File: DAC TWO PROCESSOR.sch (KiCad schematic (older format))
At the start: 99 parts

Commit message: Added outline, mounting holes and annotated components.
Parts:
- added H1, H2: MountingHole_Pad, symbol Mechanical:MountingHole_Pad
- J1: renamed from J?; symbol SciLib:CONN_20 -> DAC-TWO-PROCESSOR-rescue:CONN_20-SciLib
- J2: renamed from J?; symbol SciLib:CONN_10x2 -> DAC-TWO-PROCESSOR-rescue:CONN_10x2-SciLib
- J3: renamed from J?; symbol SciLib:CONN_10 -> DAC-TWO-PROCESSOR-rescue:CONN_10-SciLib
- U1: renamed from U?; symbol SciLib:ADP5070 -> DAC-TWO-PROCESSOR-rescue:ADP5070-SciLib
- U10: renamed from U?; symbol SciLib:LT1964-SD -> DAC-TWO-PROCESSOR-rescue:LT1964-SD-SciLib
- U11: renamed from U?; symbol SciLib:SM78L05 -> DAC-TWO-PROCESSOR-rescue:SM78L05-SciLib
- U12: renamed from U?; symbol SciLib:SM79L05 -> DAC-TWO-PROCESSOR-rescue:SM79L05-SciLib
- U2: renamed from U?; symbol SciLib:REG113-3.3 -> DAC-TWO-PROCESSOR-rescue:REG113-3.3-SciLib
- U3: renamed from U?; symbol SciLib:XTALOSC -> DAC-TWO-PROCESSOR-rescue:XTALOSC-SciLib
- U4: renamed from U?; symbol SciLib:ADP7118 -> DAC-TWO-PROCESSOR-rescue:ADP7118-SciLib
- U5: renamed from U?; symbol SciLib:AT25160B -> DAC-TWO-PROCESSOR-rescue:AT25160B-SciLib
- U6: renamed from U?; symbol SciLib:ADP7182 -> DAC-TWO-PROCESSOR-rescue:ADP7182-SciLib
- U7: renamed from U?; symbol SciLib:STM32F7xx -> DAC-TWO-PROCESSOR-rescue:STM32F7xx-SciLib
- U8, U9: renamed from U?; symbol SciLib:LT1763CS8 -> DAC-TWO-PROCESSOR-rescue:LT1763CS8-SciLib
- UX1: renamed from UX?; symbol SciLib:LT1010CN -> DAC-TWO-PROCESSOR-rescue:LT1010CN-SciLib
- gave numbers to parts that had none: 83
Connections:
- no-connect marks 34 -> 36

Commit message: Pushing footprints
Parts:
- U3: footprint CB3 -> (none)
- UX1: footprint DIP8P -> (none)
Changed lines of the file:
@@
 F 0 "U3" H 6050 2587 60  0000 C CNN
 F 1 "XX MHz" H 6050 2481 60  0000 C CNN
-F 2 "CB3" H 6050 1900 60  0001 C CNN
+F 2 "" H 6050 1900 60  0001 C CNN
 F 3 "std_library/doc/discrete/CTS CB3 OSC.pdf" H 6050 2587 60  0001 C CNN
 F 4 "11690" H 6050 2481 60  0001 C CNN "Partnum"
@@
 F 0 "UX1" H 15800 6250 60  0000 L CNN
 F 1 "LT1010CN" H 15800 6150 60  0000 L CNN
-F 2 "DIP8P" H 16050 5900 60  0001 C CNN
+F 2 "" H 16050 5900 60  0001 C CNN
 F 3 "std_library/doc/linear-tec/LT1010fc.pdf" H 16144 5947 60  0001 L CNN
 F 4 "11005" H 16144 5894 60  0001 L CNN "Partnum"

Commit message: Starting layout. Initial Commit.
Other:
- note added: "This footprint is wrong pinout! \nCorrect if using 8-lead LFCSP"
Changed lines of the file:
@@
 F 1 "LT1763CS8" H 9550 6774 50  0000 C CNN
 F 2 "" H 9550 6400 50  0001 C CNN
-F 3 "" H 9550 6400 50  0001 C CNN
+F 3 "https://www.analog.com/media/en/technical-documentation/data-sheets/1763fh.pdf" H 9550 6400 50  0001 C CNN
 	1    9550 6400
 	1    0    0    -1
@@
 F 1 "LT1964-SD" H 9675 10124 50  0000 C CNN
 F 2 "" H 9650 9700 50  0001 C CNN
-F 3 "" H 9650 9700 50  0001 C CNN
+F 3 "https://www.analog.com/media/en/technical-documentation/data-sheets/1964fb.pdf" H 9650 9700 50  0001 C CNN
 	1    9650 9700
 	1    0    0    -1
@@
 F 1 "LT1763CS8" H 9550 8424 50  0000 C CNN
 F 2 "" H 9550 8050 50  0001 C CNN
-F 3 "" H 9550 8050 50  0001 C CNN
+F 3 "https://www.analog.com/media/en/technical-documentation/data-sheets/1763fh.pdf" H 9550 8050 50  0001 C CNN
 	1    9550 8050
 	1    0    0    -1
@@
 NoConn ~ 1000 4600
 NoConn ~ 1000 5000
+Text Notes 5750 8550 0    59   Italic 12
+This footprint is wrong pinout! \nCorrect if using 8-lead LFCSP
 $EndSCHEMATC

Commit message: Layed out some more power rails. Need to TRIPLE check the EPAD connections. Many are incorrectly pinned.
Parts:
- removed U4: ADP7118, SciMod:ADP7118ARDZ, symbol DAC-TWO-PROCESSOR-rescue:ADP7118-SciLib
- added U4: ADP7118, Package_SO:SOIC-8-1EP_3.9x4.9mm_P1.27mm_EP2.35x2.35mm, symbol SciLib:ADP7118
- H1, H2: footprint (none) -> MountingHole:MountingHole_5mm_Pad_Via
- U10: footprint (none) -> SciMod:SOT23-5
- U8, U9: footprint (none) -> SciMod:SO-8_S
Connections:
- wire segments 559 -> 558
- no-connect marks 36 -> 34
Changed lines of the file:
@@
 NoConn ~ 15700 8300
-$Comp
-L DAC-TWO-PROCESSOR-rescue:ADP7118-SciLib U4
-U 1 1 5DE8A806
-P 6400 6750
-F 0 "U4" H 6500 7165 50  0000 C CNN
-F 1 "ADP7118" H 6500 7074 50  0000 C CNN
-F 2 "SciMod:ADP7118ARDZ" H 6400 6750 50  0001 C CNN
-F 3 "" H 6400 6750 50  0001 C CNN
-	1    6400 6750
-	1    0    0    -1
-$EndComp
 $Comp
 L DAC-TWO-PROCESSOR-rescue:ADP7182-SciLib U6
@@
 F 0 "U8" H 9550 6865 50  0000 C CNN
 F 1 "LT1763CS8" H 9550 6774 50  0000 C CNN
-F 2 "" H 9550 6400 50  0001 C CNN
+F 2 "SciMod:SO-8_S" H 9550 6400 50  0001 C CNN
 F 3 "https://www.analog.com/media/en/technical-documentation/data-sheets/1763fh.pdf" H 9550 6400 50  0001 C CNN
 	1    9550 6400
@@
 F 0 "U10" H 9675 10215 50  0000 C CNN
 F 1 "LT1964-SD" H 9675 10124 50  0000 C CNN
-F 2 "" H 9650 9700 50  0001 C CNN
+F 2 "SciMod:SOT23-5" H 9650 9700 50  0001 C CNN
 F 3 "https://www.analog.com/media/en/technical-documentation/data-sheets/1964fb.pdf" H 9650 9700 50  0001 C CNN
 	1    9650 9700
@@
 F 0 "U9" H 9550 8515 50  0000 C CNN
 F 1 "LT1763CS8" H 9550 8424 50  0000 C CNN
-F 2 "" H 9550 8050 50  0001 C CNN
+F 2 "SciMod:SO-8_S" H 9550 8050 50  0001 C CNN
 F 3 "https://www.analog.com/media/en/technical-documentation/data-sheets/1763fh.pdf" H 9550 8050 50  0001 C CNN
 	1    9550 8050
@@
 Connection ~ 10550 7200
 Wire Wire Line
-	10900 8500 10900 8550
-Wire Wire Line
 	10900 8800 10550 8800
-Connection ~ 10900 8550
 Wire Wire Line
 	10900 8550 10900 8800
@@
 F 0 "H2" H 1100 4949 50  0000 L CNN
 F 1 "MountingHole_Pad" H 1100 4858 50  0000 L CNN
-F 2 "" H 1000 4900 50  0001 C CNN
+F 2 "MountingHole:MountingHole_5mm_Pad_Via" H 1000 4900 50  0001 C CNN
 F 3 "~" H 1000 4900 50  0001 C CNN
 	1    1000 4900
@@
 F 0 "H1" H 1100 4549 50  0000 L CNN
 F 1 "MountingHole_Pad" H 1100 4458 50  0000 L CNN
-F 2 "" H 1000 4500 50  0001 C CNN
+F 2 "MountingHole:MountingHole_5mm_Pad_Via" H 1000 4500 50  0001 C CNN
 F 3 "~" H 1000 4500 50  0001 C CNN
 	1    1000 4500
 	1    0    0    -1
 $EndComp
-NoConn ~ 1000 4600
-NoConn ~ 1000 5000
 Text Notes 5750 8550 0    59   Italic 12
 This footprint is wrong pinout! \nCorrect if using 8-lead LFCSP
+$Comp
+L DAC-TWO-PROCESSOR-rescue:CM_GND-SciLib #PWR0158
+U 1 1 5DDC1768
+P 1000 5000
+F 0 "#PWR0158" H 1000 5050 40  0001 C CNN
+F 1 "CM_GND" H 986 5083 60  0001 C CNN
+F 2 "" H 1000 5000 60  0000 C CNN
+F 3 "" H 1000 5000 60  0000 C CNN
+	1    1000 5000
+	1    0    0    -1
+$EndComp
+$Comp
+L DAC-TWO-PROCESSOR-rescue:CM_GND-SciLib #PWR0159
+U 1 1 5DE1B7ED
+P 1000 4600
+F 0 "#PWR0159" H 1000 4650 40  0001 C CNN
+F 1 "CM_GND" H 986 4683 60  0001 C CNN
+F 2 "" H 1000 4600 60  0000 C CNN
+F 3 "" H 1000 4600 60  0000 C CNN
+	1    1000 4600
+	1    0    0    -1
+$EndComp
+$Comp
+L SciLib:ADP7118 U4
+U 1 1 5DFCFB62
+P 6400 6750
+F 0 "U4" H 6500 7165 50  0000 C CNN
+F 1 "ADP7118" H 6500 7074 50  0000 C CNN
+F 2 "Package_SO:SOIC-8-1EP_3.9x4.9mm_P1.27mm_EP2.35x2.35mm" H 6400 6750 50  0001 C CNN
+F 3 "" H 6400 6750 50  0001 C CNN
+	1    6400 6750
+	1    0    0    -1
+$EndComp
 $EndSCHEMATC

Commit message: Add files via upload
Final - added testpoints, added MANF# data. Removed reconstruction filter
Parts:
- removed C14: 4.7uF, SciMod:EIA0603, symbol Device:C
- removed C15: 10uF, SciMod:EIA1210, symbol Device:C
- removed C16, C17, C27, C41, C42: .1uF, SciMod:EIA0603, symbol Device:C
- removed C18, C19: 1uF, SciMod:EIA0603, symbol Device:C
- removed C20, C21, C22, C23, C24, C25: .01uF, SciMod:EIA0603, symbol Device:C
- removed C28: 2.2uF, SciMod:EIA0603, symbol Device:C
- removed C36, C37: 10uF, SciMod:EIA0805, symbol Device:C
- removed C39, C40, C43: .33uF, SciMod:EIA0603, symbol Device:C
- removed H1, H2: MountingHole_Pad, MountingHole:MountingHole_5mm_Pad_Via, symbol Mechanical:MountingHole_Pad
- removed R13, R14: 10, SciMod:EIA0603, symbol Device:R
- removed R15: 105K, SciMod:EIA0603, symbol Device:R
- removed R16: 10K, SciMod:EIA0603, symbol Device:R
- removed R19, R27, R28, R29, R30, R31, R32, R33, R34: 10K, SciMod:EIA0805, symbol Device:R
- removed U4: ADP7118, Package_SO:SOIC-8-1EP_3.9x4.9mm_P1.27mm_EP2.35x2.35mm, symbol SciLib:ADP7118
- removed UX1: LT1010CN, symbol DAC-TWO-PROCESSOR-rescue:LT1010CN-SciLib
- added C? (x3): 10uF, SciMod:EIA0805, symbol Device:C
- added C? (x3): .1uF, SciMod:EIA0603, symbol Device:C
- added C? (x5): .01uF, SciMod:EIA0603, symbol Device:C
- added C?: 4.7uF, SciMod:EIA0603, symbol Device:C
- added C? (x2): 1uF, SciMod:EIA0603, symbol Device:C
- added C?: 2.2uF, SciMod:EIA0603, symbol Device:C
- added C? (x3): .33uF, SciMod:EIA0603, symbol Device:C
- added R? (x9): 10K, SciMod:EIA0805, symbol Device:R
- added R? (x2): 10, SciMod:EIA0603, symbol Device:R
- added R?: 105K, SciMod:EIA0603, symbol Device:R
- added R?: 10K, SciMod:EIA0603, symbol Device:R
- added TP?: VOUT1, TESTPOINT, symbol SciLib:TST
- added TP?: +2.5V, TESTPOINT, symbol SciLib:TST
- added TP?: +8V, TESTPOINT, symbol SciLib:TST
- added TP?: -3V, TESTPOINT, symbol SciLib:TST
- added TP?: VOUT2, TESTPOINT, symbol SciLib:TST
- added U?: ADP7118, SciMod:ADP7118ARDZ, symbol SciLib:ADP7118
- C?: renamed from C4; footprint SciMod:EIA1210 -> SciMod:EIA0805; Field5 (none) -> 10µF ±10% 10V Ceramic Capacitor X7R 0805; MANF# (none) -> GRM21BR71A106KA73K
- C?: renamed from C2; Field5 (none) -> CAP CER 0.1UF 25V X8R 0603; MANF# (none) -> C1608X8R1E104K080AA
- C?: renamed from C13; Field5 (none) -> 10000pF ±5% 50V Ceramic Capacitor X7R 0805; MANF# (none) -> C0805C103J5RAC7210
- C?: renamed from C38; MANF# (none) -> CC0603KRX7R7BB334
- C?: renamed from C1; Field5 (none) -> 1µF ±20% 16V Ceramic Capacitor X7R 0603; MANF# (none) -> CL10B105MO8NNWC
- C?: renamed from C3; Field5 (none) -> 10µF Molded Tantalum Capacitors 10V 0805; MANF# (none) -> TACH106M010XTA
- C?: renamed from C7; Field4 (none) -> 2238 867 15279
- C?: renamed from C10; MANF# (none) -> 0603YC223KAT2A
- C?: renamed from C8; MANF# (none) -> CC0603JRNP09BN220
- C?: renamed from C9; MANF# (none) -> C3216X7R1H475M160AC
- C?: renamed from C6; MANF# (none) -> JMK107B7105MA
- C?: renamed from C5; MANF# (none) -> C3216X7R1E225K
- C?: renamed from C12; MANF# (none) -> C3216X7R1E225K
- C?: renamed from C11; MANF# (none) -> CL10B823KO8NNNC
- C?: renamed from C29; MANF# (none) -> GRM21BR71E225KA73L
- C?: renamed from C26; Field4 (none) -> C0603C475K9PACTU; Field5 (none) -> 4.7µF ±10% 6.3V Ceramic Capacitor X5R 0603
- C?: renamed from C35; MANF# (none) -> GRM21BR71A106KA73K
- D?: renamed from D2; MANF# (none) -> DFLS130-7
- D?: renamed from D1; MANF# (none) -> BAT54LPS
- J?: renamed from J2; symbol DAC-TWO-PROCESSOR-rescue:CONN_10x2-SciLib -> SciLib:CONN_10x2; MANF# (none) -> FTSH-110-01-L-DV; Mfg Pn FTSH-110-01-L-DV -> (none); Partnum 12133 -> (none)
- J?: renamed from J1; symbol DAC-TWO-PROCESSOR-rescue:CONN_20-SciLib -> SciLib:CONN_20; MANF# (none) -> Scientech supplied & installed; Mfg SCIENTECH -> (none)
- J?: renamed from J3; symbol DAC-TWO-PROCESSOR-rescue:CONN_10-SciLib -> SciLib:CONN_10; Description ?????? -> (none); MANF# (none) -> Scientech supplied & installed; Partnum XXXXX -> (none)
- L?: renamed from L4; MANF# (none) -> XFL4020-152MEB
- L?: renamed from L2; MANF# (none) -> LPS6235-153MRB
- L?: renamed from L1; MANF# (none) -> LPS6235-682MRB
- L?: renamed from L3; MANF# (none) -> LPS4018-222MRB
- R?: renamed from R20; Field5 (none) -> 10 kOhms ±5% 0.125W, 1/8W Chip Resistor 0805; MANF# (none) -> RMCF0805JT10K0
- R?: renamed from R1; Field5 (none) -> 30.1 kOhms ±1% 0.1W, 1/10W Chip Resistor 0603; MANF# (none) -> ERJ-3EKF3012V
- R?: renamed from R2; Field5 (none) -> 18.7 kOhms ±1% 0.1W, 1/10W Chip Resistor 0603; MANF# (none) -> ERJ-3EKF1872V
- R?: renamed from R3; Field5 (none) -> 49.9 kOhms ±1% 0.1W, 1/10W Chip Resistor 0603; MANF# (none) -> ERJ-3EKF4992V
- R?: renamed from R6; MANF# (none) -> CRCW060322K0FKEA
- R?: renamed from R7; MANF# (none) -> ERJ-3EKF3012V
- R?: renamed from R9; Field4 (none) -> ERJ-3RQF4R7V
- R?: renamed from R10; MANF# (none) -> ERJ2RKF6342X
- R?: renamed from R11; MANF# (none) -> ERJ-2RKF3571X
- R?: renamed from R4; MANF# (none) -> ERJ-2RKF2801X
- R?: renamed from R5; MANF# (none) -> ERJ-2RKF5492X
- R?: renamed from R8; MANF# (none) -> ERJ-3EKF10R0V
- R?: renamed from R17; MANF# (none) -> ERJ-3EKF1053V
- R?: renamed from R18; MANF# (none) -> ERJ-3EKF1002V
- R?: renamed from R12; MANF# (none) -> Scientech supplied & installed
- U?: renamed from U2; symbol DAC-TWO-PROCESSOR-rescue:REG113-3.3-SciLib -> SciLib:REG113-3.3; MANF# (none) -> REG113EA-3.3; Mfg Pn REG113EA-3.3 -> (none)
- U?: renamed from U5; symbol DAC-TWO-PROCESSOR-rescue:AT25160B-SciLib -> SciLib:AT25160B; MANF# (none) -> AT25160B-XHL-B; Mfg Pn AT25160B-XHL-B -> (none)
- U?: renamed from U11; symbol DAC-TWO-PROCESSOR-rescue:SM78L05-SciLib -> SciLib:SM78L05
- U?: renamed from U12; symbol DAC-TWO-PROCESSOR-rescue:SM79L05-SciLib -> SciLib:SM79L05
- U?: renamed from U1; symbol DAC-TWO-PROCESSOR-rescue:ADP5070-SciLib -> SciLib:ADP5070; MANF# (none) -> ADP5070ACPZ-R7
- U?: renamed from U6; symbol DAC-TWO-PROCESSOR-rescue:ADP7182-SciLib -> SciLib:ADP7182; Field4 (none) -> ADP7182ACPZN
- U?: renamed from U8; footprint SciMod:SO-8_S -> (none); symbol DAC-TWO-PROCESSOR-rescue:LT1763CS8-SciLib -> SciLib:LT1763CS8; MANF# (none) -> LT1763CS8#TRPBF
- U?: renamed from U10; footprint SciMod:SOT23-5 -> (none); symbol DAC-TWO-PROCESSOR-rescue:LT1964-SD-SciLib -> SciLib:LT1964-SD
- U?: renamed from U9; footprint SciMod:SO-8_S -> (none); symbol DAC-TWO-PROCESSOR-rescue:LT1763CS8-SciLib -> SciLib:LT1763CS8; MANF# (none) -> LT1763CS8#TRPBF
- U?: renamed from U7; symbol DAC-TWO-PROCESSOR-rescue:STM32F7xx-SciLib -> SciLib:STM32F7xx; MANF# (none) -> STM32F730R8T6
- U?: renamed from U3; footprint (none) -> CB3; symbol DAC-TWO-PROCESSOR-rescue:XTALOSC-SciLib -> SciLib:XTALOSC; MANF# (none) -> Scientech supplied & installed
- renumbered C30 to C?, C33 to C?, C31 to C?, C34 to C?, C32 to C?, R23 to R?, R24 to R?, R25 to R?, R26 to R?, R21 to R?, R22 to R?
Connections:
- wire segments 558 -> 542
- no-connect marks 34 -> 32
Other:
- note added: "From the AD5791 EVAL board."
- note added: "From the DC2222A LTC2500-32 A/D eval schematic"
- note removed: "This footprint is wrong pinout! \nCorrect if using 8-lead LFCSP"

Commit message: Added footpritn associations.
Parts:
- TP1, TP2, TP3, TP4, TP5: renamed from TP?; footprint TESTPOINT -> TestPoint:TestPoint_Keystone_5010-5014_Multipurpose
- U10: renamed from U?; footprint (none) -> SciMod:SOT23-5
- U3: renamed from U?; footprint CB3 -> SciMod:CB3
- U4: renamed from U?; symbol SciLib:ADP7118 -> DAC-TWO-PROCESSOR-rescue:ADP7118-SciLib
- U8, U9: renamed from U?; footprint (none) -> SciMod:SO-8_S
- gave numbers to parts that had none: 90
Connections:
- wire segments 542 -> 541

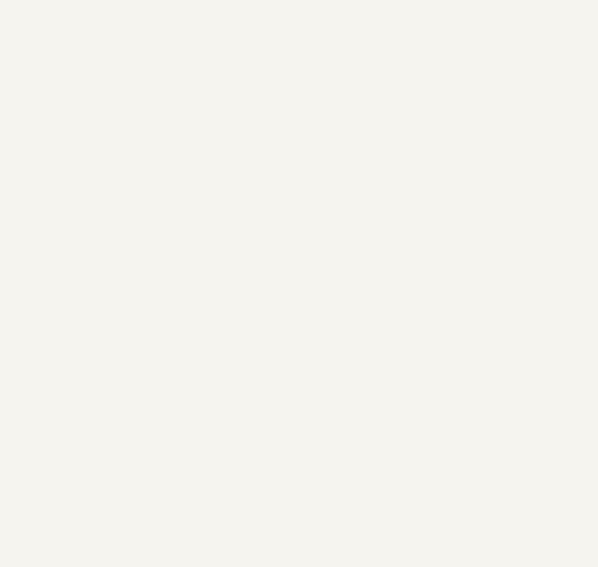
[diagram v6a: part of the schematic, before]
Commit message: Layout and placement of most switchers complete.
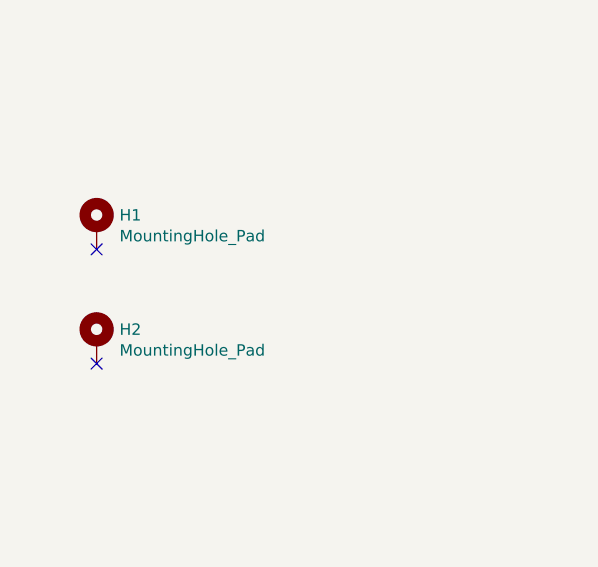
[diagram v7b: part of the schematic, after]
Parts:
- added H1, H2: MountingHole_Pad, MountingHole:MountingHole_3.2mm_M3_Pad, symbol Mechanical:MountingHole_Pad
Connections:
- no-connect marks 32 -> 34
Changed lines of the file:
@@
 Wire Wire Line
 	10900 7900 10900 8250
+$Comp
+L Mechanical:MountingHole_Pad H2
+U 1 1 5DE414E3
+P 1000 4900
+F 0 "H2" H 1100 4949 50  0000 L CNN
+F 1 "MountingHole_Pad" H 1100 4858 50  0000 L CNN
+F 2 "MountingHole:MountingHole_3.2mm_M3_Pad" H 1000 4900 50  0001 C CNN
+F 3 "~" H 1000 4900 50  0001 C CNN
+	1    1000 4900
+	1    0    0    -1
+$EndComp
+$Comp
+L Mechanical:MountingHole_Pad H1
+U 1 1 5DE42678
+P 1000 4400
+F 0 "H1" H 1100 4449 50  0000 L CNN
+F 1 "MountingHole_Pad" H 1100 4358 50  0000 L CNN
+F 2 "MountingHole:MountingHole_3.2mm_M3_Pad" H 1000 4400 50  0001 C CNN
+F 3 "~" H 1000 4400 50  0001 C CNN
+	1    1000 4400
+	1    0    0    -1
+$EndComp
+NoConn ~ 1000 5000
+NoConn ~ 1000 4500
 $EndSCHEMATC

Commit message: Added the analog portion to the board. Added as schematic sheet.
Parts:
- removed H1, H2: MountingHole_Pad, MountingHole:MountingHole_3.2mm_M3_Pad, symbol Mechanical:MountingHole_Pad
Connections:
- no-connect marks 34 -> 32
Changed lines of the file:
@@
 $Descr B 17000 11000
 encoding utf-8
-Sheet 1 1
+Sheet 1 2
 Title ""
 Date ""
@@
 Wire Wire Line
 	10900 7900 10900 8250
-$Comp
-L Mechanical:MountingHole_Pad H2
-U 1 1 5DE414E3
-P 1000 4900
-F 0 "H2" H 1100 4949 50  0000 L CNN
-F 1 "MountingHole_Pad" H 1100 4858 50  0000 L CNN
-F 2 "MountingHole:MountingHole_3.2mm_M3_Pad" H 1000 4900 50  0001 C CNN
-F 3 "~" H 1000 4900 50  0001 C CNN
-	1    1000 4900
-	1    0    0    -1
-$EndComp
-$Comp
-L Mechanical:MountingHole_Pad H1
-U 1 1 5DE42678
-P 1000 4400
-F 0 "H1" H 1100 4449 50  0000 L CNN
-F 1 "MountingHole_Pad" H 1100 4358 50  0000 L CNN
-F 2 "MountingHole:MountingHole_3.2mm_M3_Pad" H 1000 4400 50  0001 C CNN
-F 3 "~" H 1000 4400 50  0001 C CNN
-	1    1000 4400
-	1    0    0    -1
-$EndComp
-NoConn ~ 1000 5000
-NoConn ~ 1000 4500
+$Sheet
+S 14250 5600 1000 650
+U 5E1C4ACE
+F0 "Analog Portion" 50
+F1 "DAC2 ANALOG.sch" 50
+$EndSheet
 $EndSCHEMATC
